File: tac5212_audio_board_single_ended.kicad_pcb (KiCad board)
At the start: 4 copper layers, 42 x 26.5 mm, 98 parts, among them U108 Single Buffer - 74LVC1G125GV,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, U109 3.3v LDO - TLV74133PDBVR

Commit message: update
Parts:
- added SCL109: jumper, project_fp:jumper_slice, B.Cu at (110.8, 119.0)
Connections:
- R128 pad 2: 3.3v_IDE -> Net-(SCL109-A)
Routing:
- net 3.3v_IDE: track 47.2 -> 44.9 mm
- net Net-(SCL109-A): track 0.00 -> 1.33 mm

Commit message: update
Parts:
- added NT108: NetTie_2, project_fp:NetTie-2_SMD_Pad0.2mm, B.Cu at (123.6, 118.8)
- added NT109: NetTie_2, project_fp:NetTie-2_SMD_Pad0.2mm, F.Cu at (104.2, 109.6)
- D116: footprint project_fp:R_0805_2012Metric_Pad1.20x1.40mm_HandSolder -> project_fp:D_0805_2012Metric_custom
- moved 3V108 8.14 mm to (119.0, 115.6), turned to 0 degrees
- moved PU_EN108 3.85 mm to (108.2, 118.6)
- moved C111 2.81 mm to (105.0, 118.2), turned to 180 degrees
- moved G115 1.87 mm to (105.0, 119.8)
- moved C118 1.20 mm to (125.2, 103.8)
- moved G119 0.71 mm to (121.6, 115.6), turned to 180 degrees
- moved C112 0.63 mm to (108.2, 116.6), turned to -135 degrees
- moved T*C110 0.24 mm to (114.4, 118.2), turned to -90 degrees
- moved T*C109 0.17 mm to (120.2, 118.4)
- moved C129 0.15 mm to (112.3, 116.8)
- turned U109 to 90 degrees
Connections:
- C108 pad 1: 3.3V_LDO -> 3.3V_THIN
- C109 pad 1: 3.3V_LDO -> 3.3V_THIN
- G119 pad 1: Net-(G119-A) -> Earth
- G119 pad 2: Earth -> Net-(G119-B)
- R112 pad 2: Net-(TAC108-Q1-GPO1) -> Net-(TAC108-Q1-GPO1A)
- T*C108 pad 1: 5V -> 5V_THIN
- T*C108 pad 2: Net-(G119-A) -> Net-(G119-B)
- T*C109 pad 1: 5V -> 5V_THIN
- T*C109 pad 2: Net-(G119-A) -> Net-(G119-B)
- T*C110 pad 2: Net-(G119-A) -> Net-(G119-B)
- TAC108-Q1 pad 11: Net-(TAC108-Q1-GPO1) -> Net-(TAC108-Q1-GPIO1)
- TAC108-Q1 pad 15: unconnected-(TAC108-Q1-BSTVSS-Pad15) -> GNDD
- TAC108-Q1 pad 23: Net-(TAC108-Q1-GPIO1) -> Net-(TAC108-Q1-GPO1A)
- TAC108-Q1 pad 31: 3.3V_LDO -> 3.3V_THIN
- U109 pad 1: 5V -> 5V_THIN
- U109 pad 2: Net-(G119-A) -> Net-(G119-B)
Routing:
- net EN_HELD_HIGH: track 52.7 -> 8.65 mm, vias 1 -> 0
- net 5V_THIN: track 0.00 -> 25.1 mm
- net 3.3v_IDE: track 44.9 -> 24.7 mm, vias 2 -> 1
- net 5V: track 46.7 -> 34.4 mm, vias 1 -> 2
- net Net-(G119-B): track 0.00 -> 12.1 mm
- net Net-(G119-A): track 11.9 -> 0.00 mm
- net Earth: track 195.6 -> 186.8 mm
- net Net-(PU_EN108-Pad1): track 12.4 -> 5.18 mm
- net 3.3V_A: track 13.2 -> 6.33 mm
- net 3.3V_THIN: track 0.00 -> 6.58 mm
- net 3.3V_LDO: track 44.5 -> 40.5 mm, vias 2 -> 1
- net Net-(TAC108-Q1-GPO1): track 3.68 -> 0.00 mm
- net 5212_SCL: track 60.3 -> 57.6 mm
- net GNDD: track 78.6 -> 80.5 mm
- net Net-(TAC108-Q1-ADDRA): track 23.4 -> 25.1 mm

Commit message: update
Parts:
- MCLK108: footprint project_fp:jumper_slice_disconnected -> Jumper:SolderJumper-2_P1.3mm_Open_Pad1.0x1.5mm
- SCL109: footprint project_fp:jumper_slice -> Resistor_SMD:R_0402_1005Metric_Pad0.72x0.64mm_HandSolder
- moved SCL108 1.22 mm to (92.8, 101.2)
- moved MCLK108 1.04 mm to (92.6, 99.4)
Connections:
- board_outline108 pad 7: 5212_DOUT1+ -> 5212_DIN1
- board_outline108 pad 9: 5212_DIN1 -> 5212_DOUT1+
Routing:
- net EN_HELD_HIGH: track 8.65 -> 35.5 mm, vias 0 -> 1
- net GNDD: track 80.5 -> 107.0 mm, vias 12 -> 16
- net 3.3v_IDE: track 24.7 -> 48.0 mm, vias 1 -> 3
- net 5212_SCL: track 57.6 -> 53.7 mm
- net 5212_DIN1: track 25.0 -> 21.5 mm
- net GPI1: track 69.9 -> 71.5 mm
- net Net-(TAC108-Q1-GPO1A): track 0.00 -> 1.47 mm, vias 0 -> 1
- net Net-(TAC108-Q1-ADDRA): track 25.1 -> 26.4 mm
- net Net-(PU_EN108-Pad1): track 5.18 -> 6.31 mm
- net DSP_SCL: track 2.29 -> 3.41 mm
- net 5212_MCLK1: track 1.86 -> 2.84 mm
- net 5212_DOUT1+: track 12.9 -> 11.9 mm
- net Net-(TAC108-Q1-GPI2A): track 10.6 -> 9.68 mm
- net Net-(TAC108-Q1-GPIO1): track 15.3 -> 14.6 mm, vias 2 -> 3
- net Earth: track 186.8 -> 186.2 mm

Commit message: finish wqfn
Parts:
- moved NT109 0.38 mm to (104.6, 109.6)
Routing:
- net 5V_THIN: track 25.1 -> 5.67 mm
- net Net-(TAC108-Q1-GPO1A): track 1.47 -> 9.48 mm, vias 1 -> 2
- net 3.3V_THIN: track 6.58 -> 5.71 mm

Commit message: UPDATE
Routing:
- net Net-(TAC108-Q1-GPIO1): track 14.2 -> 2.50 mm, vias 3 -> 0
- net Net-(TAC108-Q1-GPO1A): track 9.48 -> 15.4 mm
- net GNDD: track 107.0 -> 105.2 mm
- net Net-(TAC108-Q1-ADDRA): track 26.4 -> 25.0 mm
- net 3.3V_LDO: track 40.8 -> 41.5 mm

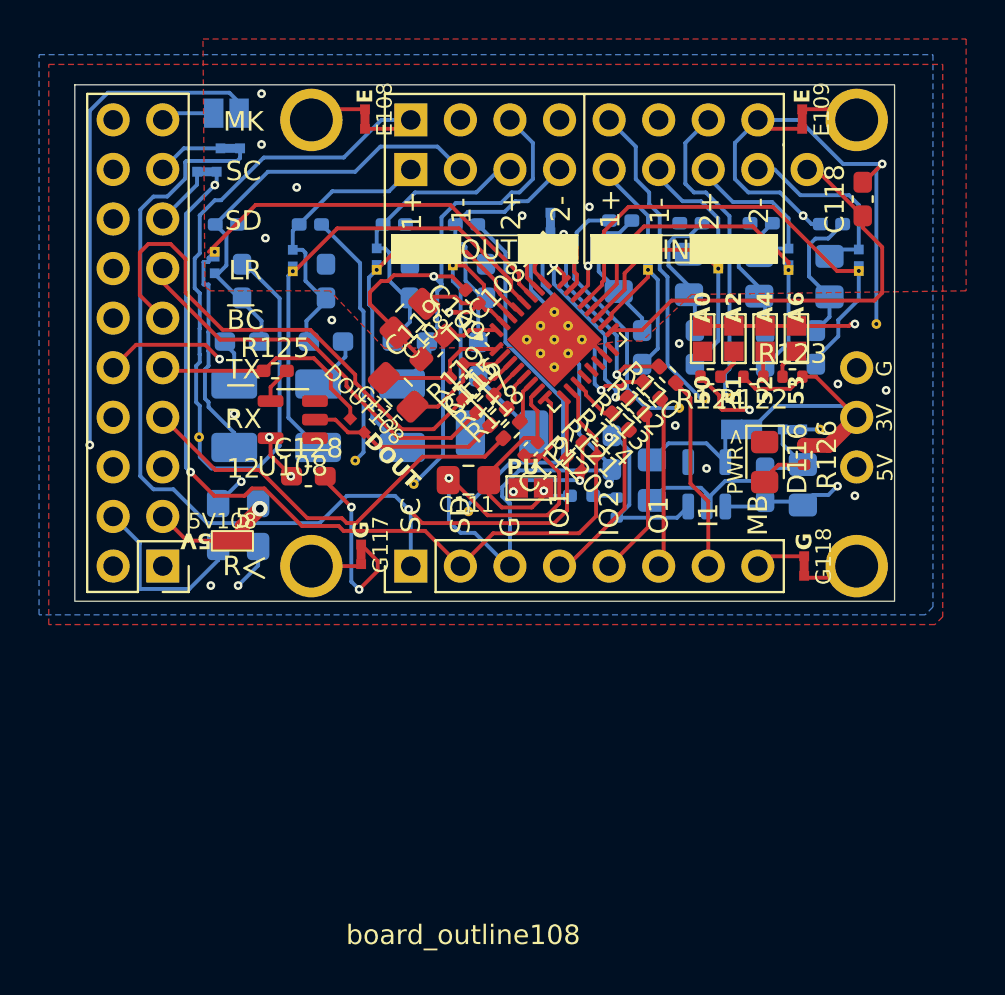
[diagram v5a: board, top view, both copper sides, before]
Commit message: fix net ties and 28 pin wqfn-28
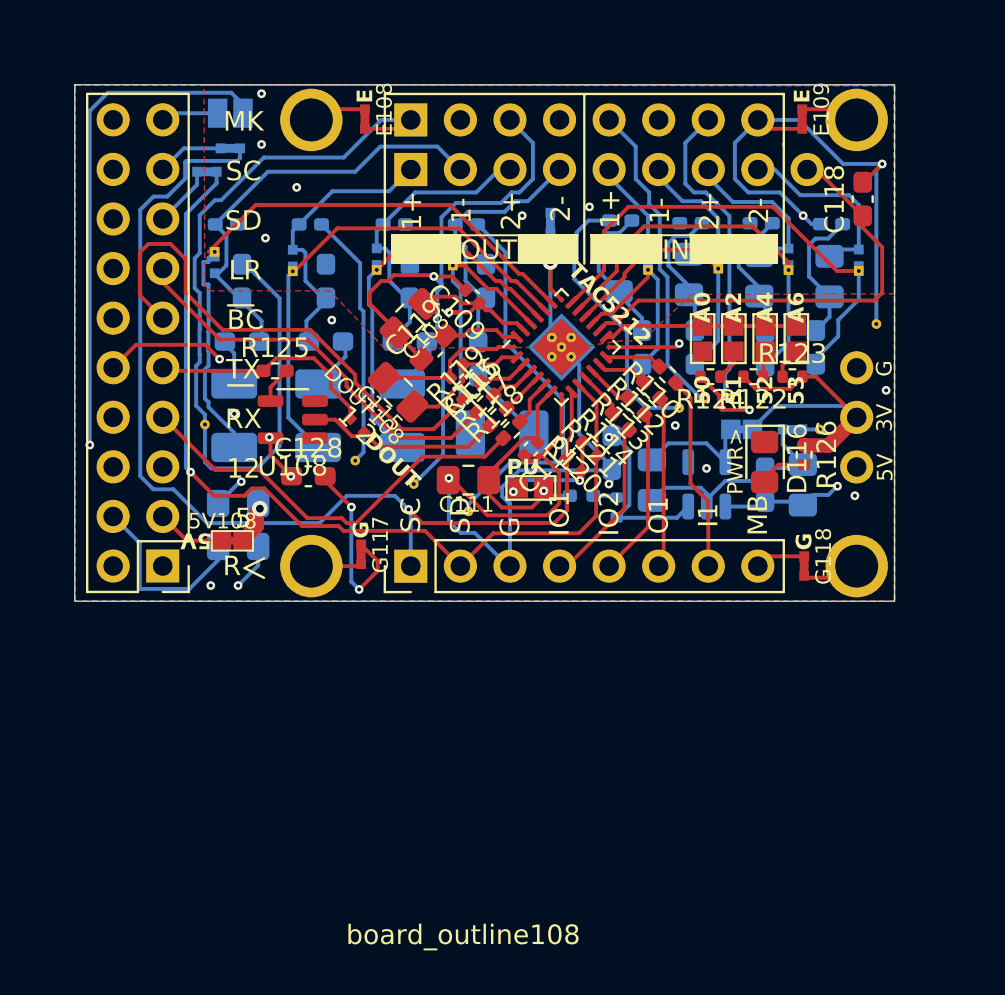
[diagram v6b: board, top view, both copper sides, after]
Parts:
- removed TAC108-Q1: TAC5212-Q1, Package_DFN_QFN:Texas_RHB0032E_VQFN-32-1EP_5x5mm_P0.5mm_EP3.45x3.45mm_ThermalVias
- added TAC5212: TAC5212, project_fp:VQFN-24-1EP_4x4mm_P0.5mm_EP2.45x2.45mm_ThermalVias, F.Cu at (109.8, 111.4)
- C109, C112, C116: footprint Capacitor_SMD:C_0402_1005Metric -> project_fp:C_0402_1005Metric
- C110, C114, C120, C122: footprint Capacitor_Tantalum_SMD:CP_EIA-3528-21_Kemet-B_Pad1.50x2.35mm_HandSolder -> project_fp:CP_EIA-3528-21_Kemet-B_Pad1.50x2.35mm_HandSolder
- C113, C117, C118, C119, C121, C123, C124, C125, C126, C127, C128, C129, T*C109: footprint Capacitor_SMD:C_0603_1608Metric_Pad1.08x0.95mm_HandSolder -> project_fp:C_0603_1608Metric_Pad1.08x0.95mm_HandSolder
- R110, R112, R113, R114, R115, R117, R118, R119, R125: footprint Resistor_SMD:R_0402_1005Metric_Pad0.72x0.64mm_HandSolder -> project_fp:R_0402_1005Metric_Pad0.72x0.64mm_HandSolder
- R120, R121, R122, R123, R124, R126, R128: footprint Resistor_SMD:R_0402_1005Metric -> project_fp:R_0402_1005Metric
- moved G111 0.72 mm to (91.5, 115.3)
- moved MCLK108 0.20 mm to (92.8, 99.4)
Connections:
- GND108 pad 1: GNDD -> unconnected-(GND108-Pad1)
- GND108 pad 2: Earth -> unconnected-(GND108-Pad2)
- SCL108 pad 1: DSP_SCL -> unconnected-(SCL108-Pad1)
- SCL108 pad 2: 5212_SCL -> unconnected-(SCL108-Pad2)
- SDA108 pad 1: DSP_SDA -> unconnected-(SDA108-Pad1)
- SDA108 pad 2: 5212_SDA -> unconnected-(SDA108-Pad2)
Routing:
- net Net-(TAC5212-ADDR): track 25.0 -> 9.98 mm, vias 2 -> 0
- net Net-(TAC5212-GPO1): track 15.4 -> 2.65 mm, vias 2 -> 0
- net Net-(TAC5212-GPI1): track 12.5 -> 2.91 mm, vias 2 -> 0
- net Net-(TAC5212-GPIO2): track 9.83 -> 2.39 mm, vias 2 -> 0
- net GNDD: track 105.2 -> 108.7 mm, vias 16 -> 15
- net Net-(TAC5212-VREF): track 2.74 -> 3.93 mm
- net 3.3V_THIN: track 5.71 -> 6.87 mm
- net OUT2M: track 12.9 -> 13.9 mm
- net OUT2P: track 19.0 -> 20.0 mm
- net OUT1P: track 24.2 -> 25.2 mm
- net OUT1M: track 31.1 -> 32.0 mm
- net Net-(TAC5212-FSYNC): track 1.82 -> 2.52 mm
- net Net-(TAC5212-DREG): track 6.24 -> 6.90 mm
- net Net-(TAC5212-BCLK): track 1.94 -> 2.60 mm
- net MICBIAS: track 22.8 -> 23.5 mm
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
